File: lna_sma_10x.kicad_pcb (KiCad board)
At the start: 2 copper layers, 0 parts

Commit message: PCB Placement, setup for 4 layers
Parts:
- added C1: 10u, Capacitor_SMD:C_1206_3216Metric_Pad1.33x1.80mm_HandSolder, F.Cu at (113.6, 66.9)
- added C2: 160p, Capacitor_SMD:C_1206_3216Metric_Pad1.33x1.80mm_HandSolder, F.Cu at (111.1, 82.7)
- added C3: 0.1u, Capacitor_SMD:C_1206_3216Metric_Pad1.33x1.80mm_HandSolder, F.Cu at (115.5, 55.1)
- added C4: 0.1u, Capacitor_SMD:C_1206_3216Metric_Pad1.33x1.80mm_HandSolder, F.Cu at (120.8, 82.5)
- added C5: 10u, Capacitor_SMD:C_1206_3216Metric_Pad1.33x1.80mm_HandSolder, F.Cu at (113.7, 73.1)
- added C6: 0.1u, Capacitor_SMD:C_1206_3216Metric_Pad1.33x1.80mm_HandSolder, F.Cu at (128.2, 59.6)
- added C7: 0.1u, Capacitor_SMD:C_1206_3216Metric_Pad1.33x1.80mm_HandSolder, F.Cu at (129.2, 76.7)
- added J1: Conn_Coaxial, Connector_Coaxial:SMA_Amphenol_132289_EdgeMount, F.Cu at (103.6, 81.5)
- added J2: Power In, Connector_Molex:Molex_Nano-Fit_105313-xx03_1x03_P2.50mm_Horizontal, F.Cu at (109.5, 72.2)
- added J3: Conn_Coaxial, Connector_Coaxial:SMA_Amphenol_132289_EdgeMount, F.Cu at (103.0, 58.1)
- added R1: 10K, Resistor_SMD:R_1206_3216Metric_Pad1.30x1.75mm_HandSolder, F.Cu at (109.2, 78.5)
- added R2: 10K, Resistor_SMD:R_1206_3216Metric_Pad1.30x1.75mm_HandSolder, F.Cu at (113.3, 78.6)
- added R3: 50R, Resistor_SMD:R_1206_3216Metric_Pad1.30x1.75mm_HandSolder, F.Cu at (116.8, 78.6)
- added R4: 500R, Resistor_SMD:R_1206_3216Metric_Pad1.30x1.75mm_HandSolder, F.Cu at (118.4, 69.0)
- added R5: 3K3, Resistor_SMD:R_1206_3216Metric_Pad1.30x1.75mm_HandSolder, F.Cu at (122.6, 67.0)
- added R6: 100R, Resistor_SMD:R_1206_3216Metric_Pad1.30x1.75mm_HandSolder, F.Cu at (127.2, 66.3)
- added R7: 1k2, Resistor_SMD:R_1206_3216Metric_Pad1.30x1.75mm_HandSolder, F.Cu at (120.1, 63.5)
- added R8: 50R, Resistor_SMD:R_1206_3216Metric_Pad1.30x1.75mm_HandSolder, F.Cu at (111.4, 59.6)
- added U1: LT1722xS8, Package_SO:SOIC-8_3.9x4.9mm_P1.27mm, F.Cu at (123.3, 75.5)
- added U2: BUF602xD, Package_SO:SOIC-8_3.9x4.9mm_P1.27mm, F.Cu at (122.2, 57.7)
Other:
- copper layers 2 -> 4

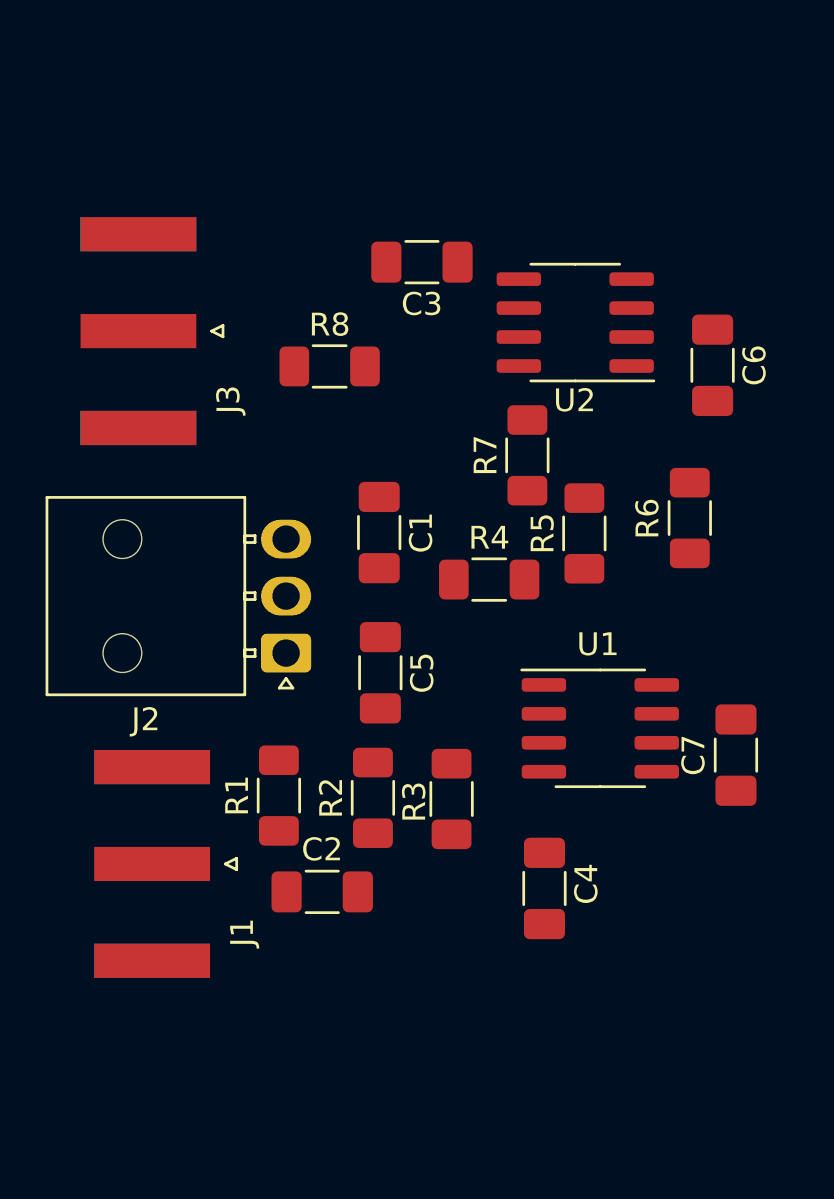
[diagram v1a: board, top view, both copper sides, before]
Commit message: Defined PCB edges and holes
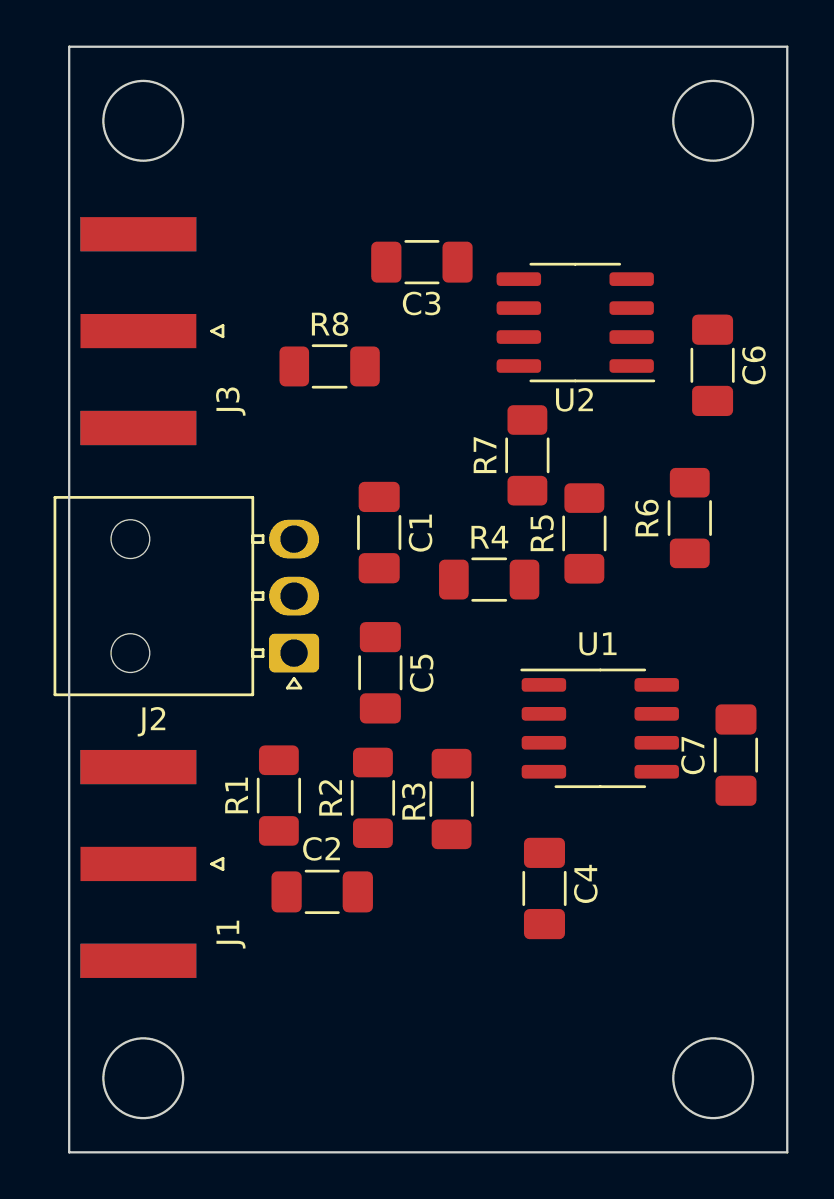
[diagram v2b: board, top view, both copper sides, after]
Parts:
- moved J1 0.60 mm to (103.0, 81.5)
- moved J2 0.35 mm to (109.9, 72.2)
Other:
- board outline added: 31.5 x 48.5 mm
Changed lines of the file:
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@@
     )
     (pad_to_mask_clearance 0)
+    (grid_origin 103.25 48.875)
     (pcbplotparams
       (layerselection 0x00010fc_ffffffff)
@@
     )
   )
-  (footprint "Connector_Coaxial:SMA_Amphenol_132289_EdgeMount" (layer "F.Cu")
-    (at 103.6375 81.475 180)
+  (footprint "Connector_Coaxial:SMA_Amphenol_132289_EdgeMount" locked (layer "F.Cu")
+    (at 103.037488 81.474996 180)
     (descr "http://www.amphenolrf.com/132289.html")
     (tags "SMA")
@@
     (fp_line (start 3.54 0) (end 2.54 0.75) (layer "F.Fab") (width 0.1))
     (fp_line (start 4.445 -3.81) (end 4.445 -5.08) (layer "F.Fab") (width 0.1))
-    (pad "1" smd rect (at 0 0 270) (size 1.5 5.08) (layers "F.Cu" "F.Paste" "F.Mask")
+    (pad "1" smd rect locked (at 0 0 270) (size 1.5 5.08) (layers "F.Cu" "F.Paste" "F.Mask")
       (net 11 "/sig_in") (pinfunction "In") (pintype "passive"))
-    (pad "2" smd rect (at 0 -4.25 270) (size 1.5 5.08) (layers "F.Cu" "F.Paste" "F.Mask")
+    (pad "2" smd rect locked (at 0 -4.25 270) (size 1.5 5.08) (layers "F.Cu" "F.Paste" "F.Mask")
       (net 2 "GND") (pinfunction "Ext") (pintype "passive"))
-    (pad "2" smd rect (at 0 4.25 270) (size 1.5 5.08) (layers "B.Cu" "B.Paste" "B.Mask")
+    (pad "2" smd rect locked (at 0 4.25 270) (size 1.5 5.08) (layers "B.Cu" "B.Paste" "B.Mask")
       (net 2 "GND") (pinfunction "Ext") (pintype "passive"))
-    (pad "2" smd rect (at 0 -4.25 270) (size 1.5 5.08) (layers "B.Cu" "B.Paste" "B.Mask")
+    (pad "2" smd rect locked (at 0 -4.25 270) (size 1.5 5.08) (layers "B.Cu" "B.Paste" "B.Mask")
       (net 2 "GND") (pinfunction "Ext") (pintype "passive"))
-    (pad "2" smd rect (at 0 4.25 270) (size 1.5 5.08) (layers "F.Cu" "F.Paste" "F.Mask")
+    (pad "2" smd rect locked (at 0 4.25 270) (size 1.5 5.08) (layers "F.Cu" "F.Paste" "F.Mask")
       (net 2 "GND") (pinfunction "Ext") (pintype "passive"))
     (model "${KICAD6_3DMODEL_DIR}/Connector_Coaxial.3dshapes/SMA_Amphenol_132289_EdgeMount.wrl"
@@
     )
   )
-  (footprint "Connector_Coaxial:SMA_Amphenol_132289_EdgeMount" (layer "F.Cu")
+  (footprint "Connector_Coaxial:SMA_Amphenol_132289_EdgeMount" locked (layer "F.Cu")
     (at 103.0375 58.1 180)
     (descr "http://www.amphenolrf.com/132289.html")
@@
     (fp_line (start 3.54 0) (end 2.54 0.75) (layer "F.Fab") (width 0.1))
     (fp_line (start -1.91 -5.08) (end -1.91 -3.81) (layer "F.Fab") (width 0.1))
-    (pad "1" smd rect (at 0 0 270) (size 1.5 5.08) (layers "F.Cu" "F.Paste" "F.Mask")
+    (pad "1" smd rect locked (at 0 0 270) (size 1.5 5.08) (layers "F.Cu" "F.Paste" "F.Mask")
       (net 13 "/sig_out") (pinfunction "In") (pintype "passive"))
-    (pad "2" smd rect (at 0 -4.25 270) (size 1.5 5.08) (layers "F.Cu" "F.Paste" "F.Mask")
+    (pad "2" smd rect locked (at 0 -4.25 270) (size 1.5 5.08) (layers "F.Cu" "F.Paste" "F.Mask")
       (net 2 "GND") (pinfunction "Ext") (pintype "passive"))
-    (pad "2" smd rect (at 0 -4.25 270) (size 1.5 5.08) (layers "B.Cu" "B.Paste" "B.Mask")
+    (pad "2" smd rect locked (at 0 -4.25 270) (size 1.5 5.08) (layers "B.Cu" "B.Paste" "B.Mask")
       (net 2 "GND") (pinfunction "Ext") (pintype "passive"))
-    (pad "2" smd rect (at 0 4.25 270) (size 1.5 5.08) (layers "B.Cu" "B.Paste" "B.Mask")
+    (pad "2" smd rect locked (at 0 4.25 270) (size 1.5 5.08) (layers "B.Cu" "B.Paste" "B.Mask")
       (net 2 "GND") (pinfunction "Ext") (pintype "passive"))
-    (pad "2" smd rect (at 0 4.25 270) (size 1.5 5.08) (layers "F.Cu" "F.Paste" "F.Mask")
+    (pad "2" smd rect locked (at 0 4.25 270) (size 1.5 5.08) (layers "F.Cu" "F.Paste" "F.Mask")
       (net 2 "GND") (pinfunction "Ext") (pintype "passive"))
     (model "${KICAD6_3DMODEL_DIR}/Connector_Coaxial.3dshapes/SMA_Amphenol_132289_EdgeMount.wrl"
@@
     )
   )
-  (footprint "Connector_Molex:Molex_Nano-Fit_105313-xx03_1x03_P2.50mm_Horizontal" (layer "F.Cu")
-    (at 109.515 72.225 180)
+  (footprint "Connector_Molex:Molex_Nano-Fit_105313-xx03_1x03_P2.50mm_Horizontal" locked (layer "F.Cu")
+    (at 109.865 72.225 180)
     (descr "Molex Nano-Fit Power Connectors, 105313-xx03, 3 Pins per row (http://www.molex.com/pdm_docs/sd/1053131208_sd.pdf), generated with kicad-footprint-generator")
     (tags "connector Molex Nano-Fit top entry")
@@
     (fp_line (start 10.38 -1.72) (end 1.92 -1.72) (layer "F.Fab") (width 0.1))
     (fp_line (start 0.3 -1.534264) (end -0.3 -1.534264) (layer "F.Fab") (width 0.1))
-    (pad "" np_thru_hole circle (at 7.18 0 180) (size 1.7 1.7) (drill 1.7) (layers *.Cu *.Mask))
-    (pad "" np_thru_hole circle (at 7.18 5 180) (size 1.7 1.7) (drill 1.7) (layers *.Cu *.Mask))
-    (pad "1" thru_hole roundrect (at 0 0 180) (size 2.2 1.7) (drill 1.2) (layers *.Cu *.Mask) (roundrect_rratio 0.147059)
+    (pad "" np_thru_hole circle locked (at 7.18 0 180) (size 1.7 1.7) (drill 1.7) (layers *.Cu *.Mask))
+    (pad "" np_thru_hole circle locked (at 7.18 5 180) (size 1.7 1.7) (drill 1.7) (layers *.Cu *.Mask))
+    (pad "1" thru_hole roundrect locked (at 0 0 180) (size 2.2 1.7) (drill 1.2) (layers *.Cu *.Mask) (roundrect_rratio 0.147059)
       (net 3 "+5V") (pinfunction "Pin_1") (pintype "power_out"))
-    (pad "2" thru_hole oval (at 0 2.5 180) (size 2.2 1.7) (drill 1.2) (layers *.Cu *.Mask)
+    (pad "2" thru_hole oval locked (at 0 2.5 180) (size 2.2 1.7) (drill 1.2) (layers *.Cu *.Mask)
       (net 2 "GND") (pinfunction "Pin_2") (pintype "power_out"))
-    (pad "3" thru_hole oval (at 0 5 180) (size 2.2 1.7) (drill 1.2) (layers *.Cu *.Mask)
+    (pad "3" thru_hole oval locked (at 0 5 180) (size 2.2 1.7) (drill 1.2) (layers *.Cu *.Mask)
       (net 1 "-5V") (pinfunction "Pin_3") (pintype "power_out"))
     (model "${KICAD6_3DMODEL_DIR}/Connector_Molex.3dshapes/Molex_Nano-Fit_105313-xx03_1x03_P2.50mm_Horizontal.wrl"
@@
     )
   )
+  (gr_circle (center 128.25 48.875) (end 131 48.875) (layer "Dwgs.User") (width 0.15) (fill none))
+  (gr_circle (center 103.25 48.875) (end 106 48.875) (layer "Dwgs.User") (width 0.15) (fill none))
+  (gr_circle (center 103.25 90.875) (end 106 90.875) (layer "Dwgs.User") (width 0.15) (fill none))
+  (gr_circle (center 128.25 90.875) (end 131 90.875) (layer "Dwgs.User") (width 0.15) (fill none))
+  (gr_rect (start 100 45.625) (end 131.5 94.125) (layer "Edge.Cuts") (width 0.1) (fill none))
+  (gr_circle (center 103.25 90.875) (end 105 90.875) (layer "Edge.Cuts") (width 0.1) (fill none))
+  (gr_circle (center 128.25 48.875) (end 130 48.875) (layer "Edge.Cuts") (width 0.1) (fill none))
+  (gr_circle (center 103.25 48.875) (end 105 48.875) (layer "Edge.Cuts") (width 0.1) (fill none))
+  (gr_circle (center 128.25 90.875) (end 130 90.875) (layer "Edge.Cuts") (width 0.1) (fill none))
+  (dimension (type orthogonal) (layer "Dwgs.User")
+    (pts (xy 100 94.125) (xy 131.5 94.125))
+    (height 9)
+    (orientation 0)
+    (gr_text "31.5000 mm" (at 115.75 101.975) (layer "Dwgs.User")
+      (effects (font (size 1 1) (thickness 0.15)))
+    )
+    (format (units 3) (units_format 1) (precision 4))
+    (style (thickness 0.1) (arrow_length 1.27) (text_position_mode 0) (extension_height 0.58642) (extension_offset 0.5) keep_text_aligned)
+  )
+  (dimension (type orthogonal) (layer "Dwgs.User")
+    (pts (xy 100 52.75) (xy 100.5 52.75))
+    (height 45.375)
+    (orientation 0)
+    (gr_text "0.5000 mm" (at 100.25 96.975) (layer "Dwgs.User")
+      (effects (font (size 1 1) (thickness 0.15)))
+    )
+    (format (units 3) (units_format 1) (precision 4))
+    (style (thickness 0.15) (arrow_length 1.27) (text_position_mode 0) (extension_height 0.58642) (extension_offset 0.5) keep_text_aligned)
+  )
+  (dimension (type orthogonal) (layer "Dwgs.User")
+    (pts (xy 128.25 48.875) (xy 128.25 90.875))
+    (height 14)
+    (orientation 1)
+    (gr_text "42.0000 mm" (at 141.1 69.875 90) (layer "Dwgs.User")
+      (effects (font (size 1 1) (thickness 0.15)))
+    )
+    (format (units 3) (units_format 1) (precision 4))
+    (style (thickness 0.1) (arrow_length 1.27) (text_position_mode 0) (extension_height 0.58642) (extension_offset 0.5) keep_text_aligned)
+  )
+  (dimension (type orthogonal) (layer "Dwgs.User")
+    (pts (xy 103.25 48.875) (xy 128.25 48.875))
+    (height 0)
+    (orientation 0)
+    (gr_text "25.0000 mm" (at 115.75 47.725) (layer "Dwgs.User")
+      (effects (font (size 1 1) (thickness 0.15)))
+    )
+    (format (units 3) (units_format 1) (precision 4))
+    (style (thickness 0.1) (arrow_length 1.27) (text_position_mode 0) (extension_height 0.58642) (extension_offset 0.5) keep_text_aligned)
+  )
+  (dimension (type orthogonal) (layer "Dwgs.User")
+    (pts (xy 131.5 45.625) (xy 131.5 94.125))
+    (height 15)
+    (orientation 1)
+    (gr_text "48.5000 mm" (at 145.35 69.875 90) (layer "Dwgs.User")
+      (effects (font (size 1 1) (thickness 0.15)))
+    )
+    (format (units 3) (units_format 1) (precision 4))
+    (style (thickness 0.1) (arrow_length 1.27) (text_position_mode 0) (extension_height 0.58642) (extension_offset 0.5) keep_text_aligned)
+  )
 )

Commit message: PCB routed and planes filled
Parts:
- turned R8 to 180 degrees
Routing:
- net GND: track 0.00 -> 47.2 mm, vias 0 -> 10
- net +5V: track 0.00 -> 13.7 mm, vias 0 -> 3
- net /buf_in: track 0.00 -> 12.7 mm
- net -5V: track 0.00 -> 12.1 mm, vias 0 -> 3
- net /amp_out: track 0.00 -> 10.8 mm
- net /sig_in: track 0.00 -> 9.28 mm
- net /buf_out: track 0.00 -> 9.22 mm
- net /fb_in: track 0.00 -> 9.05 mm
- net /sig_out: track 0.00 -> 7.23 mm
- net /sig_in_ac: track 0.00 -> 6.20 mm
- net /amp_in: track 0.00 -> 4.28 mm
- net /R5toR7: track 0.00 -> 2.58 mm
- added copper zone on In1.Cu, net +5V
- added copper zone on In2.Cu, net -5V
- added copper zone on B.Cu, net GND

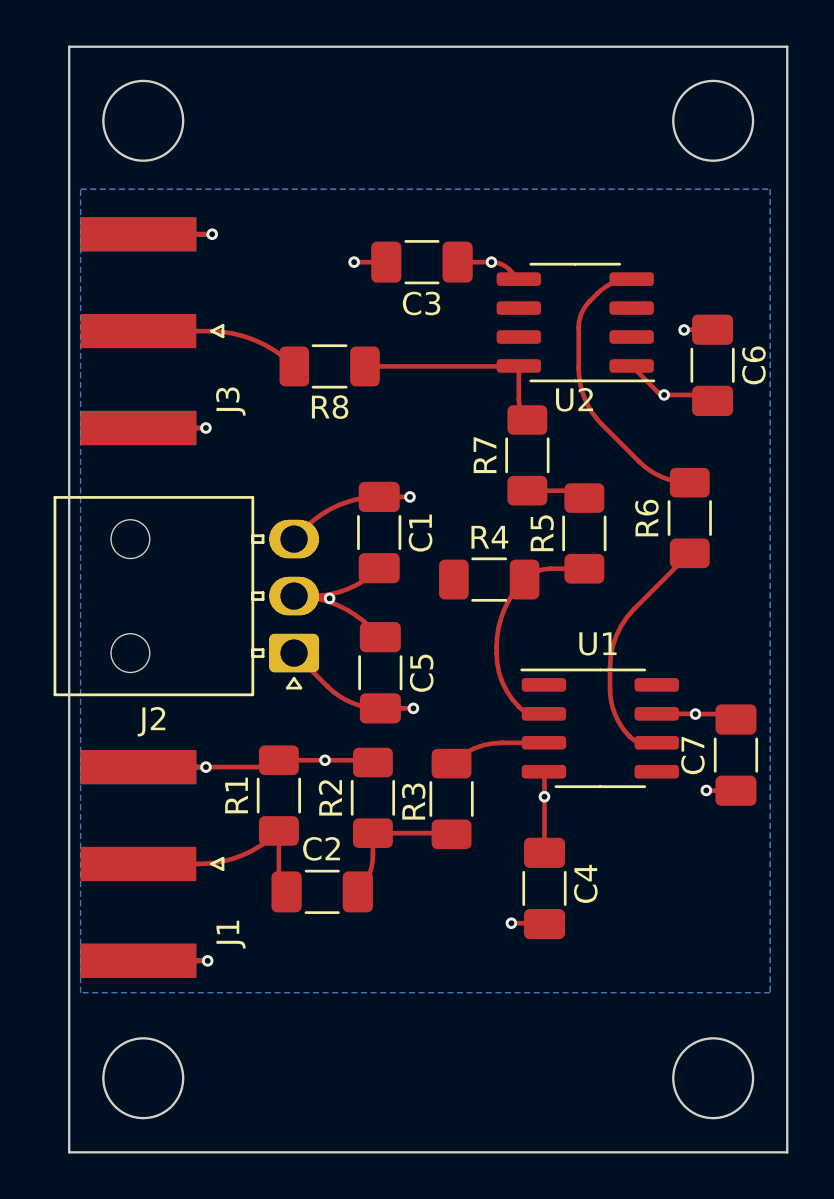
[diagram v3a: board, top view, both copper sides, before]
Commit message: completed silkscreen and bumped to 1.0
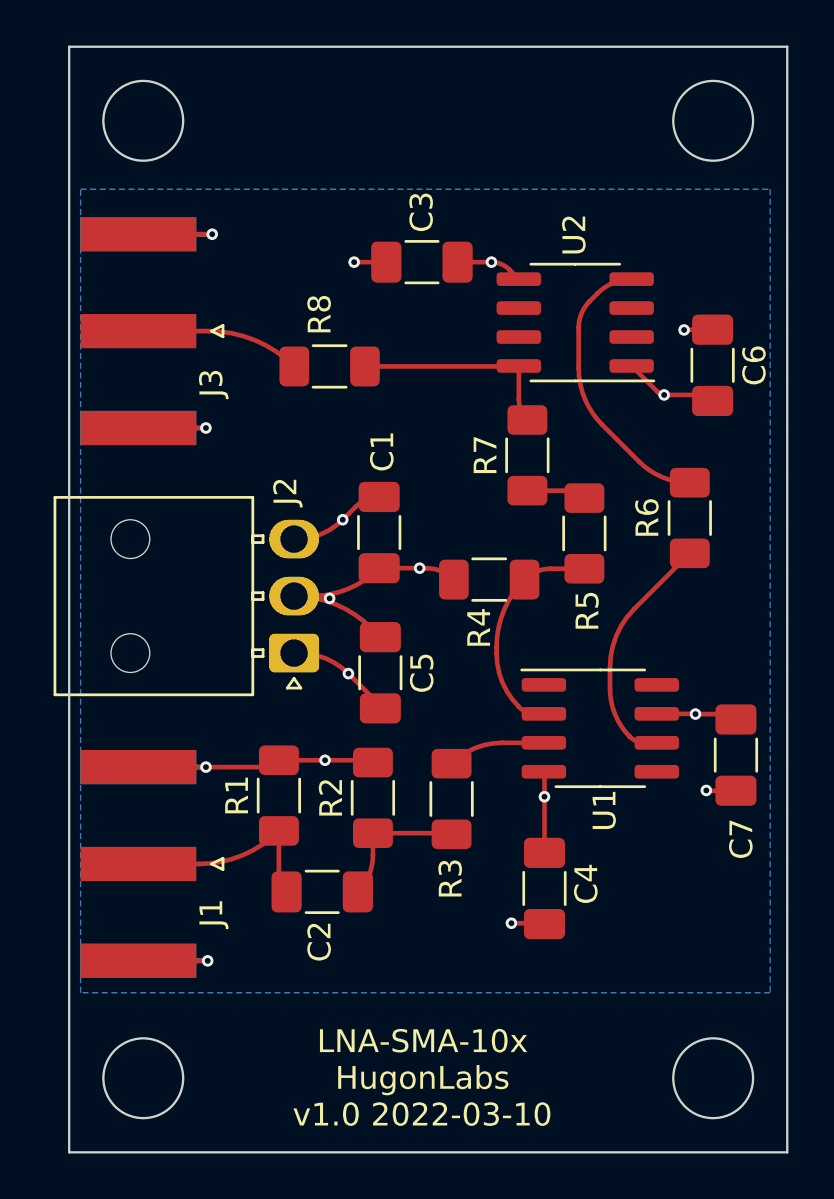
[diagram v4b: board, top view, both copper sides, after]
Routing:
- net GND: track 47.2 -> 50.6 mm, vias 10 -> 11
- net -5V: track 12.1 -> 10.7 mm
- net +5V: track 13.7 -> 12.4 mm
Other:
- board text added: "0"
- board text added: "0 mm"
- board text added: "0.017272 mm"
- board text added: "0.02"
- board text added: "0.0254 mm"
- board text added: "0.04318 mm"
- board text added: "0.1270 mm / 0.1270 mm"
- board text added: "0.202184 mm"
- board text added: "0.2540 mm"
- board text added: "1"
- board text added: "1.1938 mm"
- board text added: "1.7699 mm"
- board text added: "3.3"
- board text added: "31.6000 mm x 48.6000 mm"
- board text added: "4"
- board text added: "4.5"
- board text added: "B.Cu"
- board text added: "B.Mask"
- board text added: "B.Paste"
- board text added: "B.Silkscreen"
- board text added: "BOARD CHARACTERISTICS"
- board text added: "Board Thickness:"
- board text added: "Board overall dimensions:"
- board text added: "Bottom Silk Screen"
- board text added: "Bottom Solder Mask"
- board text added: "Bottom Solder Paste"
- board text added: "Castellated pads:"
- board text added: "Color"
- board text added: "Copper Finish:"
- board text added: "Copper Layer Count:"
- board text added: "Dielectric 1"
- board text added: "Dielectric 2"
- board text added: "Dielectric 3"
- board text added: "Edge card connectors:"
- board text added: "Epsilon R"
- board text added: "F.Cu"
- board text added: "F.Mask"
- board text added: "F.Paste"
- board text added: "F.Silkscreen"
- board text added: "FR4"
- board text added: "Impedance Control:"
- board text added: "In1.Cu"
- board text added: "In2.Cu"
- board text added: "LNA-SMA-10x HugonLabs v1.0 2022-03-10"
- board text added: "Layer Name"
- board text added: "Loss Tangent"
- board text added: "Material"
- board text added: "Min hole diameter:"
- board text added: "Min track/spacing:"
- board text added: "No"
- board text added: "None"
- board text added: "Not specified"
- board text added: "Plated Board Edge:"
- board text added: "Purple"
- board text added: "Thickness (mm)"
- board text added: "Top Silk Screen"
- board text added: "Top Solder Mask"
- board text added: "Top Solder Paste"
- board text added: "Type"
- board text added: "White"
- board text added: "copper"
- board text added: "core"
- board text added: "prepreg"
